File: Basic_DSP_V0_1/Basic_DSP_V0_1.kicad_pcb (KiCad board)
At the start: 2 copper layers, 60 x 100 mm, 183 parts, among them J1 53048-0310, J10 53048-0310, J11 53048-0410, J12 Conn_ARM_SWD_TagConnect_TC2030, J13 USB_C_Receptacle, J14 53048-0210, J15 53048-0210, J16 Conn_02x08_Odd_Even, J2 53048-0310, J3 53048-0310, J4 53048-0310, J5 53048-0310, J6 53048-0410, J7 53048-0310, J8 53048-0310, J9 53048-0310, Q1 AO3400A, Q2 AO3400A, Q3 AO3400A, U1 STM32F415RGTx, U10 TLV9161IDBVR, U2 CS4270, U3 TLV76733QWDRBRQ1, U5 NCP718BSN500T1G, U6 TLV9161IDBVR, U7 TLV9161IDBVR, U8 TLV9161IDBVR, U9 TLV9161IDBVR, Y1 ABM8G-24.000MHZ-18-D2Y-T3

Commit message: Basic placement on PCB
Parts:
- removed C16, C17, C18, C19, C20, C21, C22: 22u, Capacitor_SMD:C_1210_3225Metric
- added C75: 2u2, Capacitor_SMD:C_0805_2012Metric, F.Cu at (101.0, 354.0)
- added C76: 2u2, Capacitor_SMD:C_0805_2012Metric, F.Cu at (100.0, 334.0)
- moved J5 426.8 mm to (77.7, 381.8), turned to 90 degrees
- moved J4 425.3 mm to (77.7, 372.8), turned to 90 degrees
- moved D5 419.5 mm to (80.0, 383.6), turned to 90 degrees
- moved R19 419.5 mm to (83.0, 383.0), turned to 180 degrees
- moved R18 414.5 mm to (83.0, 374.0), turned to 180 degrees
- moved C31 411.7 mm to (83.0, 385.0), turned to 180 degrees
- moved D7 411.3 mm to (80.0, 374.6), turned to 90 degrees
- moved J3 408.4 mm to (77.7, 363.8), turned to 90 degrees
- moved D4 407.5 mm to (80.0, 365.6), turned to 90 degrees
- moved J2 406.9 mm to (77.7, 354.8), turned to 90 degrees
- moved C30 406.6 mm to (83.1, 376.0), turned to 180 degrees
- moved D25 402.1 mm to (80.0, 357.0), turned to 90 degrees
- moved C24 401.6 mm to (83.0, 367.0), turned to 180 degrees
- moved J10 400.2 mm to (128.3, 376.2), turned to -90 degrees
- moved J9 399.5 mm to (128.3, 368.2), turned to -90 degrees
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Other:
- board text added: "CHASE SIGNALS"

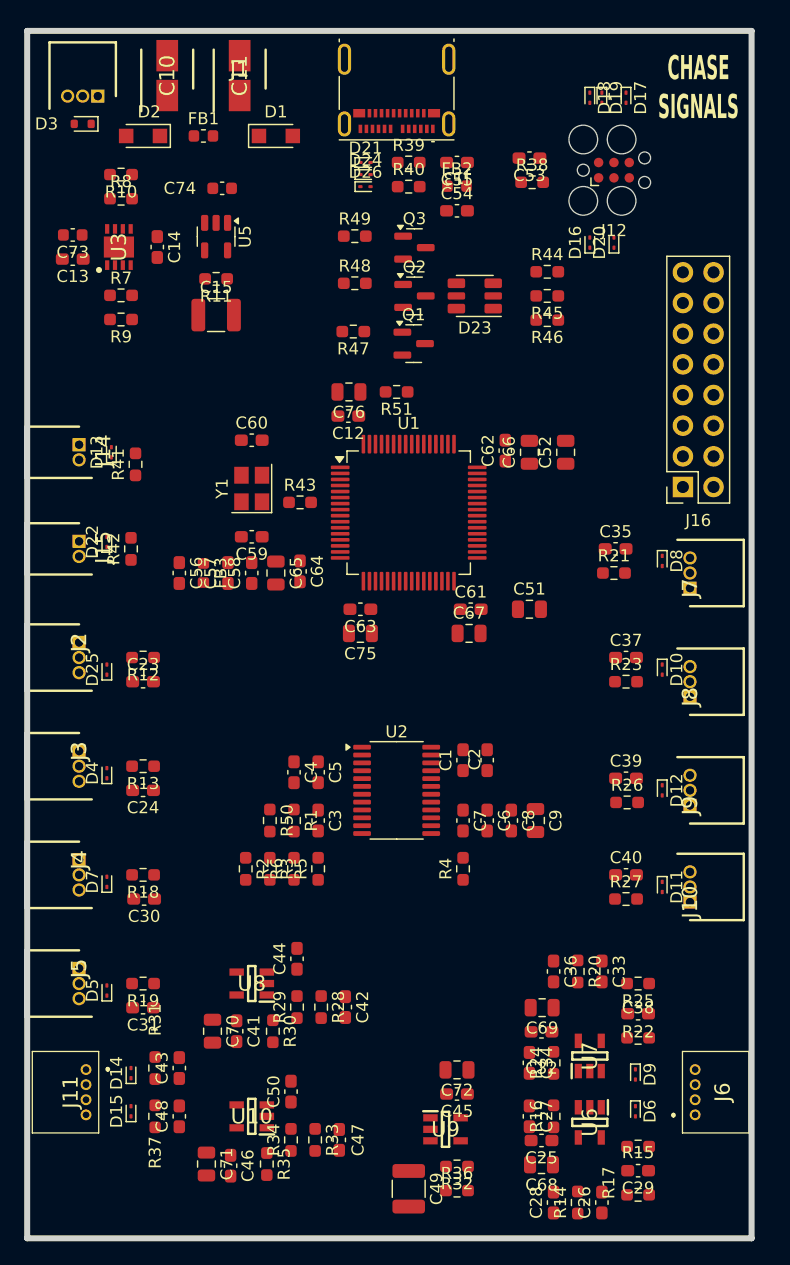
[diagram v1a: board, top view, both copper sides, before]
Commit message: Updated parts with LCSC order codes
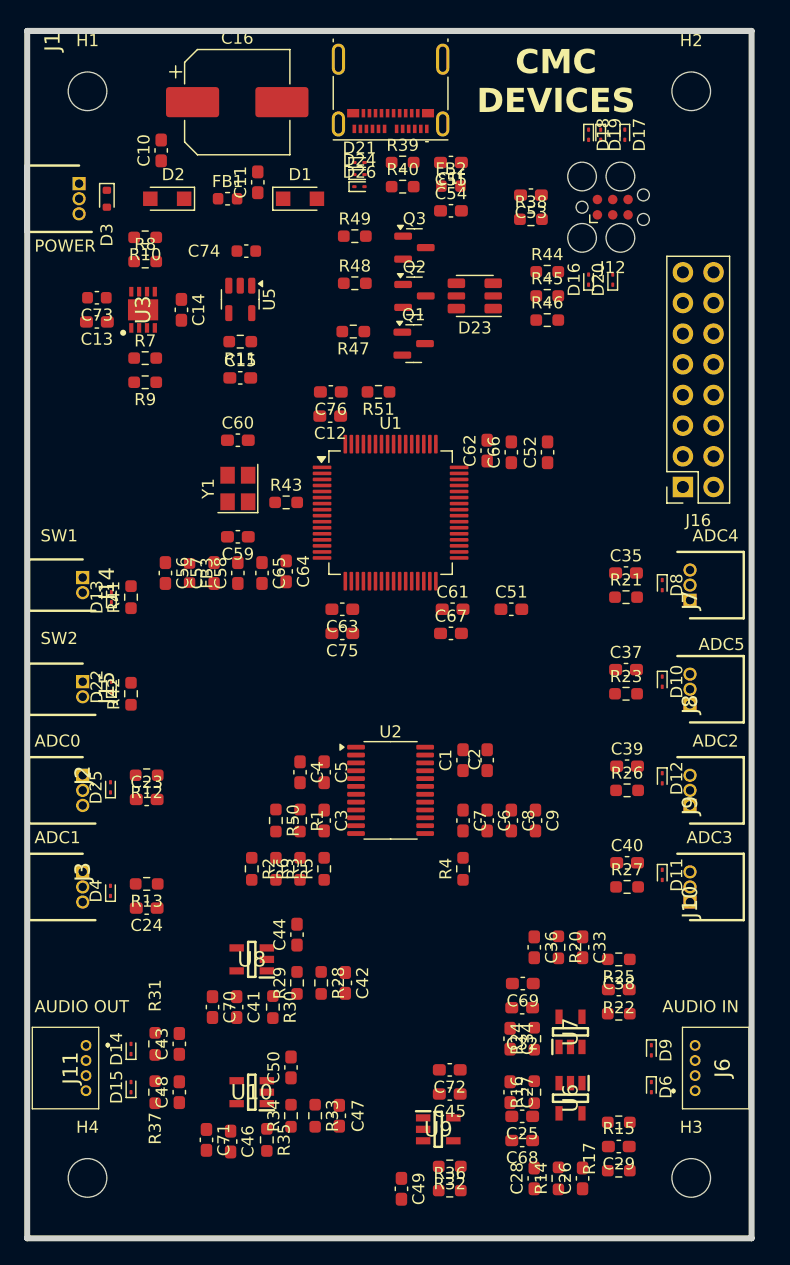
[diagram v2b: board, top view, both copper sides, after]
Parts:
- removed C30, C31: 100n, Capacitor_SMD:C_0603_1608Metric_Pad1.08x0.95mm_HandSolder
- removed D5, D7: ESD9B3.3ST5G, Diode_SMD:D_SOD-923
- removed J4, J5: 53048-0310, Chase_Conn:SHDRRA3W35P0X125_1X3_550X550X350P
- removed R18, R19: 33R, Resistor_SMD:R_0603_1608Metric_Pad0.98x0.95mm_HandSolder
- added C16: 220uF, Capacitor_SMD:CP_Elec_8x10.5, F.Cu at (90.8, 310.0)
- added H1: MountingHole, MountingHole:MountingHole_3.2mm_M3, F.Cu at (78.4, 309.1)
- added H2: MountingHole, MountingHole:MountingHole_3.2mm_M3, F.Cu at (128.4, 309.1)
- added H3: MountingHole, MountingHole:MountingHole_3.2mm_M3, F.Cu at (128.4, 399.1)
- added H4: MountingHole, MountingHole:MountingHole_3.2mm_M3, F.Cu at (78.4, 399.1)
- C10, C11: footprint Chase_Capacitor:CAPAE430X550N -> Capacitor_SMD:C_0603_1608Metric_Pad1.08x0.95mm_HandSolder
- C15, C49: footprint Capacitor_SMD:C_1210_3225Metric -> Capacitor_SMD:C_0603_1608Metric_Pad1.08x0.95mm_HandSolder
- C51, C52, C65, C66, C67, C68, C69, C70, C71, C72, C75, C76, C9: footprint Capacitor_SMD:C_0805_2012Metric -> Capacitor_SMD:C_0603_1608Metric_Pad1.08x0.95mm_HandSolder
- moved D22 12.0 mm to (80.4, 358.4)
- moved D13 12.0 mm to (80.4, 351.0)
- moved R42 12.0 mm to (82.0, 359.0)
- moved J15 11.6 mm to (78.0, 358.0)
- moved R41 11.0 mm to (82.0, 351.0)
- moved J14 11.0 mm to (78.0, 349.4)
- moved J2 11.0 mm to (78.0, 365.8)
- moved J3 10.0 mm to (78.0, 373.8)
- moved C23 9.75 mm to (83.3, 367.8)
- moved C24 9.75 mm to (83.3, 376.8)
- moved D25 9.75 mm to (80.3, 366.8)
- moved D4 9.75 mm to (80.3, 375.3)
- moved R12 9.75 mm to (83.3, 365.8)
- moved R13 9.75 mm to (83.3, 374.8)
- moved C11 8.96 mm to (92.5, 316.6)
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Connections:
- C39 pad 1: /Connections/ADC_IN6 -> /Connections/ADC_IN2
- C40 pad 1: /Connections/ADC_IN7 -> /Connections/ADC_IN3
- R26 pad 1: /Connections/ADC_IN6 -> /Connections/ADC_IN2
- R27 pad 1: /Connections/ADC_IN7 -> /Connections/ADC_IN3
- U1 pad 22: /Connections/ADC_IN6 -> unconnected-(U1-PA6-Pad22)
- U1 pad 23: /Connections/ADC_IN7 -> unconnected-(U1-PA7-Pad23)
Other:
- copper layers 2 -> 4
- board text added: "ADC0"
- board text added: "ADC1"
- board text added: "ADC2"
- board text added: "ADC3"
- board text added: "ADC4"
- board text added: "ADC5"
- board text added: "AUDIO IN"
- board text added: "AUDIO OUT"
- board text added: "CMC DEVICES"
- board text added: "POWER"
- board text added: "SW1"
- board text added: "SW2"
- board text removed: "CHASE SIGNALS"

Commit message: WIP - small layout progress on basic DSP
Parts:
- moved C36 9.53 mm to (114.6, 389.5), turned to 180 degrees
- moved C27 7.62 mm to (114.8, 399.5), turned to 0 degrees
- moved C25 6.44 mm to (110.0, 398.7), turned to -90 degrees
- moved U7 5.98 mm to (114.0, 382.9), turned to 180 degrees
- moved C69 5.85 mm to (110.0, 386.9), turned to -90 degrees
- moved R16 5.74 mm to (114.8, 397.7), turned to 180 degrees
- moved C26 5.35 mm to (118.3, 393.9), turned to 180 degrees
- moved U6 4.92 mm to (114.0, 394.7), turned to 180 degrees
- moved R32 4.82 mm to (103.7, 399.2)
- moved R36 4.80 mm to (103.7, 401.1)
- moved R20 4.16 mm to (118.5, 384.0), turned to 180 degrees
- moved C45 4.08 mm to (104.5, 393.2)
- moved C72 4.08 mm to (104.5, 391.2)
- moved C68 3.68 mm to (111.9, 398.7), turned to -90 degrees
- moved C49 3.50 mm to (100.9, 400.1)
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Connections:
- C12 pad 1: +3.3V -> +3V3
- C61 pad 1: +3.3V -> +3V3
- C62 pad 1: +3.3V -> +3V3
- C63 pad 1: +3.3V -> +3V3
- C66 pad 1: +3.3V -> +3V3
- C67 pad 1: +3.3V -> +3V3
- C75 pad 1: +3.3V -> +3V3
- C76 pad 1: +3.3V -> +3V3
- J16 pad 2: +3.3V -> +3V3
- R41 pad 1: +3.3V -> +3V3
- R42 pad 1: +3.3V -> +3V3
- U1 pad 19: +3.3V -> +3V3
- U1 pad 32: +3.3V -> +3V3
- U1 pad 48: +3.3V -> +3V3
- U1 pad 64: +3.3V -> +3V3
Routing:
- net /Analogue/AUDIO_IN_R: track 0.00 -> 8.77 mm
- net /Analogue/AUDIO_IN_L: track 0.00 -> 7.49 mm
- net Net-(C26-Pad1): track 0.00 -> 6.10 mm
- net Net-(U9-IN+): track 0.00 -> 5.97 mm
- net Net-(C33-Pad1): track 0.00 -> 5.90 mm
- net Net-(U6-IN-): track 0.00 -> 5.51 mm
- net Net-(U7-IN-): track 0.00 -> 5.43 mm
- net Net-(U7-IN+): track 0.00 -> 4.34 mm
- net Net-(U6-IN+): track 0.00 -> 3.96 mm
- net Net-(C34-Pad1): track 0.00 -> 3.32 mm
- net +VREF: track 0.00 -> 3.29 mm
- net Net-(C27-Pad1): track 0.00 -> 3.22 mm
- added copper zone on F.Cu, net +3V3
- added copper zone on F.Cu, net +5VA

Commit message: more layout work on basic DSP
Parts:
- moved C74 59.0 mm to (110.4, 378.3), turned to -90 degrees
- moved U5 57.0 mm to (114.4, 378.3), turned to 0 degrees
- moved R11 55.4 mm to (117.9, 378.3), turned to -90 degrees
- moved C15 53.8 mm to (119.8, 378.3), turned to 90 degrees
- moved R2 42.5 mm to (107.2, 333.8), turned to 0 degrees
- moved R3 39.9 mm to (107.2, 335.8), turned to 0 degrees
- moved C1 2.25 mm to (109.5, 362.2)
- moved C2 2.25 mm to (111.5, 362.2)
- moved C3 2.25 mm to (98.0, 367.2)
- moved C4 2.25 mm to (96.0, 362.6)
- moved C5 2.25 mm to (98.0, 362.6)
- moved C6 2.25 mm to (111.5, 367.2)
- moved C7 2.25 mm to (109.5, 367.2)
- moved C8 2.25 mm to (113.5, 367.2)
- moved C9 2.25 mm to (115.5, 367.2)
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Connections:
- C42 pad 1: /Analogue/CODEC_OUT_L -> /Analogue/CODEC_OUT_R
- C43 pad 2: /Analogue/AUDIO_OUT_L -> /Analogue/AUDIO_OUT_R
- C47 pad 1: /Analogue/CODEC_OUT_R -> /Analogue/CODEC_OUT_L
- C48 pad 2: /Analogue/AUDIO_OUT_R -> /Analogue/AUDIO_OUT_L
- D14 pad 2: /Analogue/AUDIO_OUT_L -> /Analogue/AUDIO_OUT_R
- D15 pad 2: /Analogue/AUDIO_OUT_R -> /Analogue/AUDIO_OUT_L
- J11 pad 1: /Analogue/AUDIO_OUT_L -> /Analogue/AUDIO_OUT_R
- J11 pad 3: /Analogue/AUDIO_OUT_R -> /Analogue/AUDIO_OUT_L
- R31 pad 2: /Analogue/AUDIO_OUT_L -> /Analogue/AUDIO_OUT_R
- R37 pad 2: /Analogue/AUDIO_OUT_R -> /Analogue/AUDIO_OUT_L
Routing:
- net /CODEC/I2S_ADC_OUT: track 0.00 -> 36.5 mm, vias 0 -> 2
- net /CODEC/I2S_WCLK: track 0.00 -> 25.9 mm, vias 0 -> 2
- net /CODEC/I2S_MCLK: track 0.00 -> 24.2 mm, vias 0 -> 2
- net /CODEC/I2S_BCLK: track 0.00 -> 21.7 mm, vias 0 -> 2
- net /CODEC/I2S_DAC_IN: track 0.00 -> 19.2 mm, vias 0 -> 2
- net Net-(C48-Pad1): track 0.00 -> 15.6 mm
- net Net-(C43-Pad1): track 0.00 -> 9.74 mm
- net /Analogue/AUDIO_OUT_R: track 0.00 -> 8.69 mm
- net /Analogue/AUDIO_OUT_L: track 0.00 -> 7.97 mm
- net /CODEC/CODEC_OUT: track 0.00 -> 5.71 mm
- net Net-(U8-IN-): track 0.00 -> 5.37 mm
- net Net-(U10-IN-): track 0.00 -> 5.37 mm
- net Net-(U8-IN+): track 0.00 -> 4.82 mm
- net Net-(U10-IN+): track 0.00 -> 4.32 mm
- net Net-(C47-Pad2): track 0.00 -> 4.02 mm
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- added copper zone on In2.Cu, net +5VA
- added copper zone on F.Cu, net +VREF
- added copper zone on In2.Cu, net +VREF
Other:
- copper layers 4 -> 6
